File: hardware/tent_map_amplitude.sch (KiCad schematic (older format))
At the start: 52 parts, among them U1 LM339AN, U2 TL082IP, U3 TL082IP, U4 LF398_DIP8, U5 LF398_DIP8, U6 LF398_DIP8

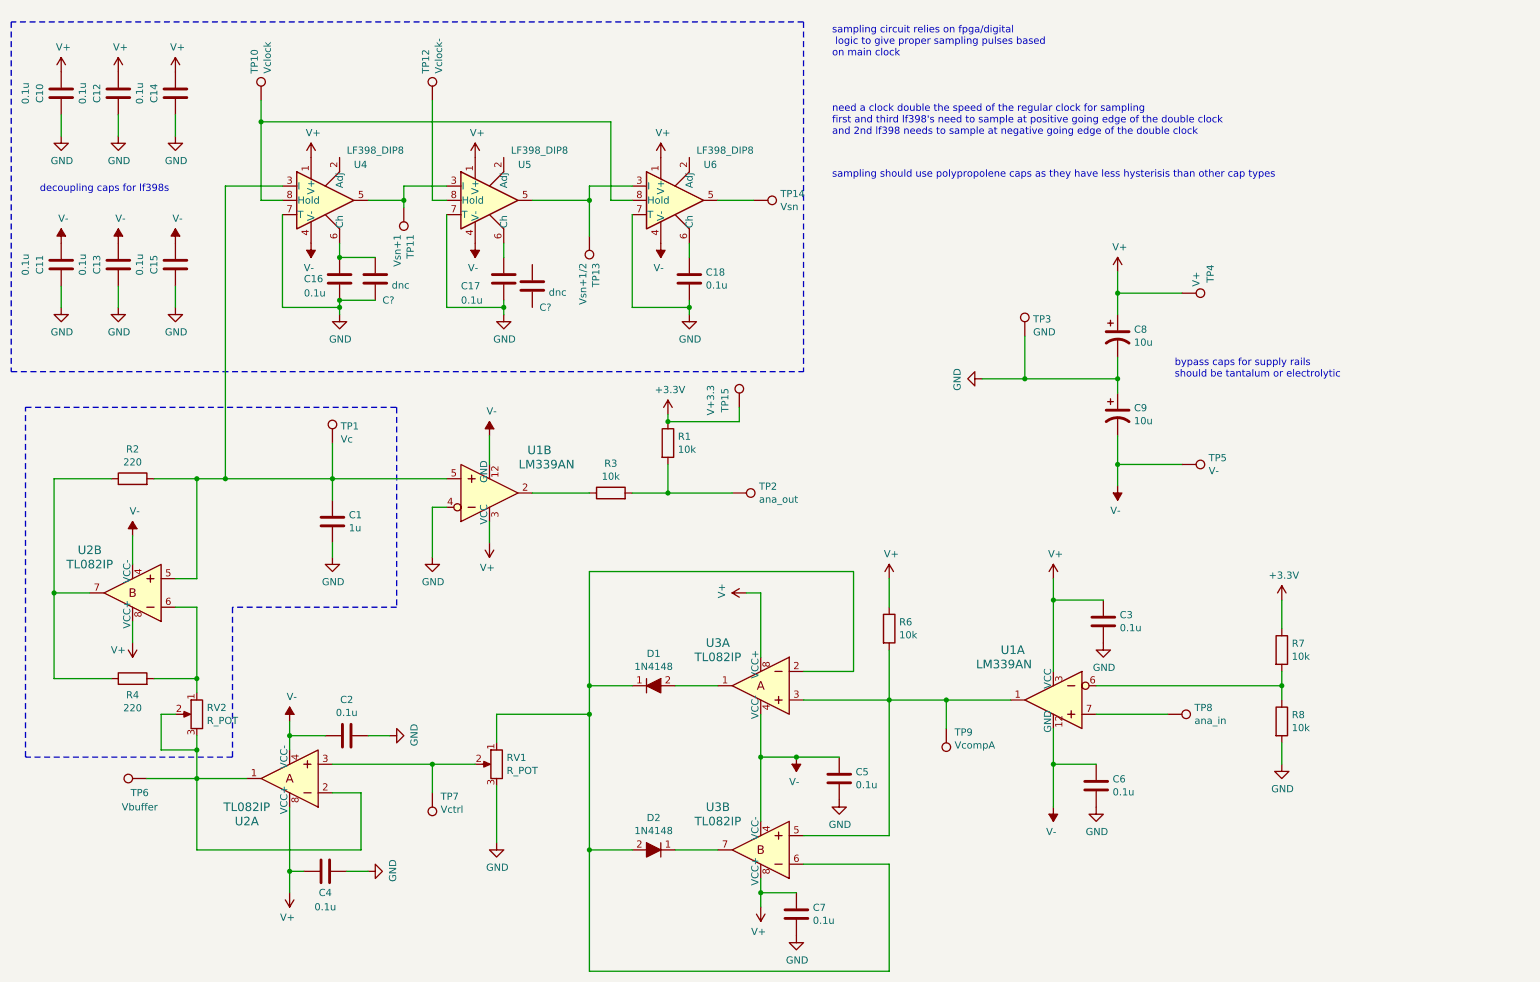
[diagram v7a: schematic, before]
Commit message: Make changes based on beal's recomendations, add extra caps on schematic for extra 0805 footprint, add unused comparator symbols
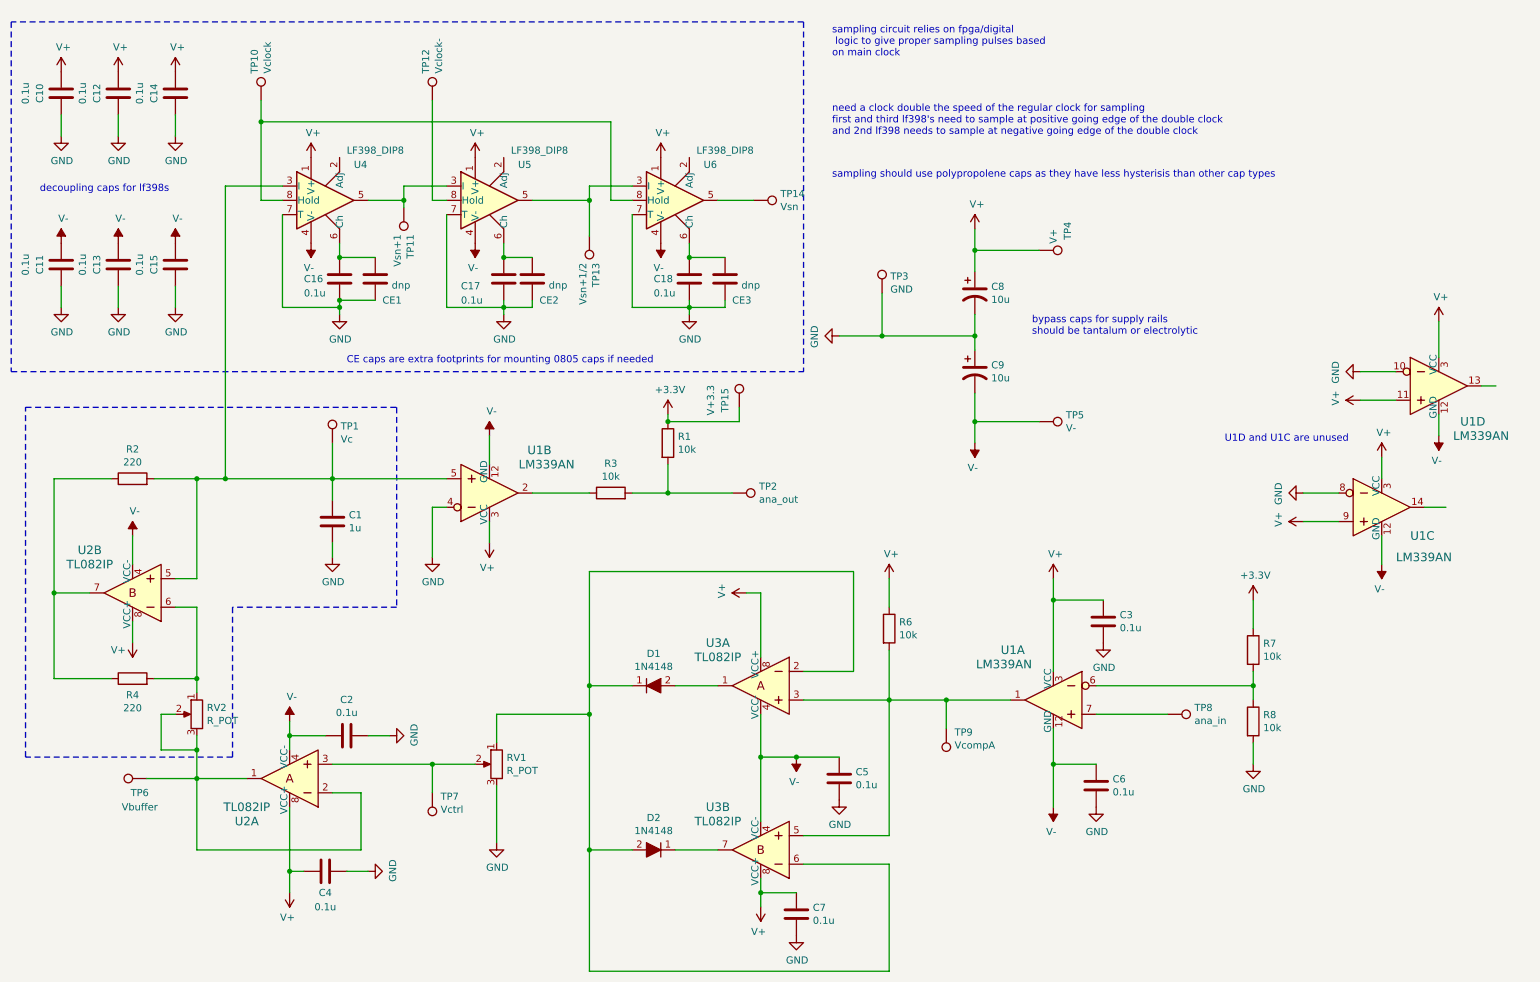
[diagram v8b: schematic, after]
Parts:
- added CE3: dnp, Capacitor_SMD:C_0805_2012Metric_Pad1.18x1.45mm_HandSolder, symbol Device:C
- added unit 3 of U1
- added unit 4 of U1
- CE1, CE2: renamed from C?; value dnc -> dnp; footprint Capacitor_THT:C_Rect_L10.3mm_W5.0mm_P7.50mm_MKS4 -> Capacitor_SMD:C_0805_2012Metric_Pad1.18x1.45mm_HandSolder
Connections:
- net GND: now also CE2.2, CE3.2, U1.10, U1.8
- net V+: now also U1.11, U1.3 (VCC), U1.3 (VCC), U1.9
- net V-: now also U1.12 (GND), U1.12 (GND)
- net at CE2.1: now also C17.1, U5.6 (Ch)
- net at C18.1, U6.6 (Ch): now also CE3.1
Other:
- note added: "CE caps are extra footprints for mounting 0805 caps if needed"
- note added: "U1D and U1C are unused"
- moved on the sheet: C8, C9, CE2, R7, R8, TP3, TP4, TP5
